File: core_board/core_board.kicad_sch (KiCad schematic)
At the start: 92 parts

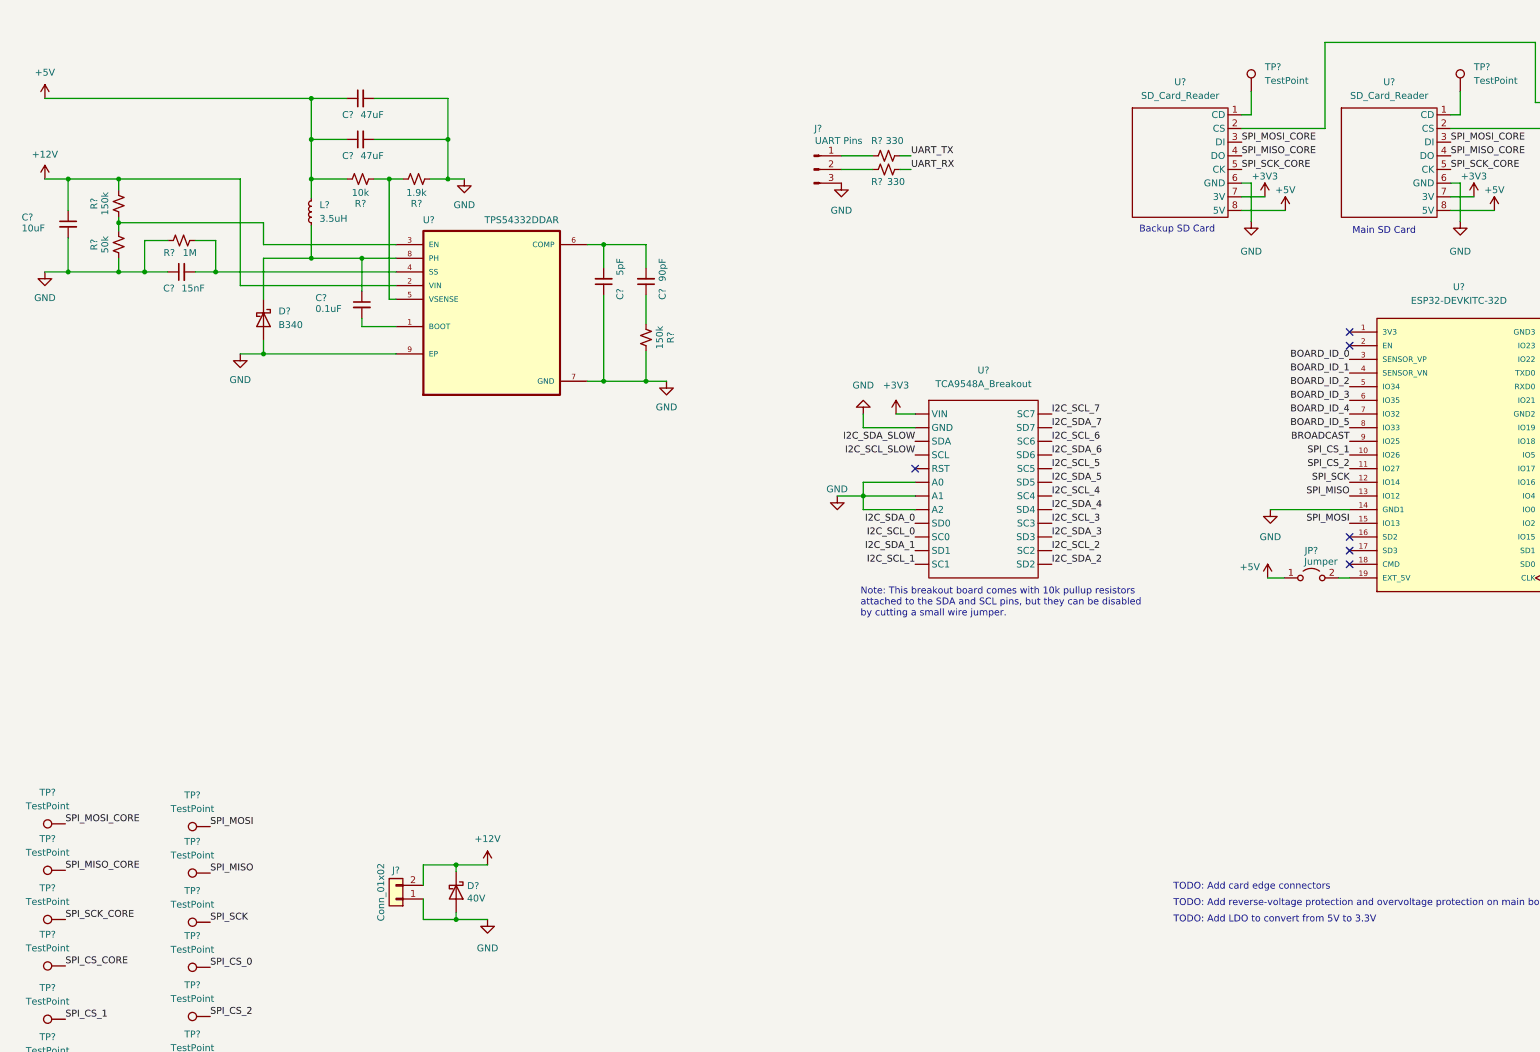
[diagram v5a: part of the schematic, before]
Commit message: added LDO
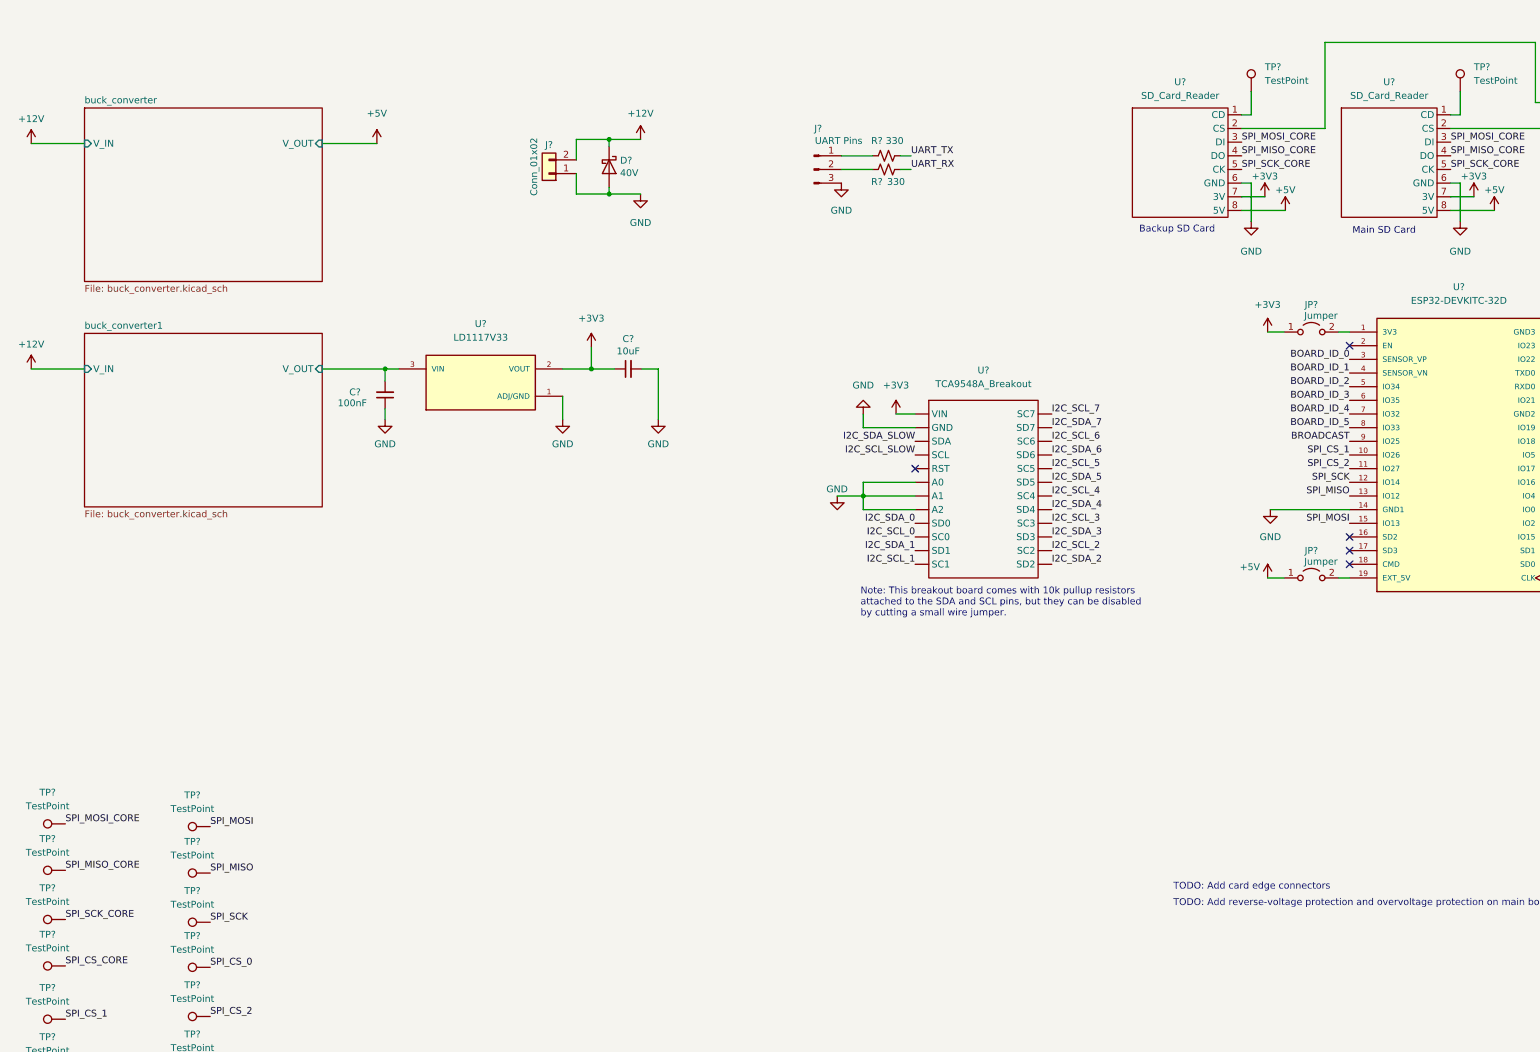
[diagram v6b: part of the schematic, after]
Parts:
- removed C? (x2): 47uF, symbol Device:C_Small
- removed C?: 90pF, symbol Device:C_Small
- removed C?: 5pF, symbol Device:C_Small
- removed C?: 10uF, symbol Device:C_Small
- removed C?: 0.1uF, symbol Device:C_Small
- removed C?: 15nF, symbol Device:C_Small
- removed D?: B340, Diode_SMD:D_SMC, symbol Diode:B340
- removed L?: 3.5uH, symbol Device:L_Small
- removed R? (x2): 150k, symbol Device:R_Small_US
- removed R?: 1M, symbol Device:R_Small_US
- removed R?: 50k, symbol Device:R_Small_US
- removed R?: 1.9k, symbol Device:R_Small_US
- removed R?: 10k, symbol Device:R_Small_US
- removed U?: TPS54332DDAR, VREG_LM5017MR/NOPB, symbol TPS54332DDAR:TPS54332DDAR
- added C?: 100nF, symbol Device:C_Small
- added C?: 10uF, symbol Device:C_Small
- added JP?: Jumper, symbol Jumper:Jumper_2_Open
- added U?: LD1117V33, TO255P1020X450X1968-3, symbol LD1117V33:LD1117V33
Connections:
- net +3V3: now also C?.1, JP?.1 (A), U?.2 (VOUT)
- net GND: now also C?.1, C?.2, U?.1 (ADJ/GND)
- net at U?.1 (3V3): now also JP?.2 (B)
- new net buck_converter1/V_OUT: C?.2, U?.3 (VIN)
- no-connect marks 11 -> 10
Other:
- added sheet buck_converter (buck_converter.kicad_sch)
- added sheet buck_converter1 (buck_converter.kicad_sch)
- note removed: "TODO: Add LDO to convert from 5V to 3.3V"
- moved on the sheet: D?, J?

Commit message: small changes
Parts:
- removed D?: 40V, Diode_SMD:D_0603_1608Metric, symbol Device:D_Schottky
- added D?: D_Zener, symbol Device:D_Zener
- added D?: D_Schottky, symbol Device:D_Schottky
- added R? (x2): 4.7k, symbol Device:R_Small_US
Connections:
- net +12V: now also D?.1 (K), D?.1 (K); no longer J?.2 (Pin_2)
- net +3V3: now also R?.2, R?.2; no longer JP?.1 (A), JP?.1 (A), U?.2 (CS), U?.2 (CS)
- net GND: now also D?.2 (A)
- new net: JP?.1 (A), R?.1, U?.2 (CS) (x2)
- new net: D?.2 (A), J?.2 (Pin_2)
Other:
- note removed: "TODO: Add card edge connectors"
- note removed: "TODO: Add reverse-voltage protection and overvoltage protection on main board"
- moved on the sheet: C?, J?, JP?, R?, TP?, U?

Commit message: added PCIE connectors
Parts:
- removed C?: 10uF, symbol Device:C_Small
- added C?: 10uF, symbol Device:C_Small
- added J? (x8): PCIE-LP-01-01-F-DV-A-TR, SAMTEC_PCIE-LP-01-01-F-DV-A-TR, symbol PCIE_Socket:PCIE-LP-01-01-F-DV-A-TR
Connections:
- net +12V: now also J?.A16, J?.A16, J?.A16, J?.A16, J?.A16, J?.A16, J?.A16, J?.A16, J?.A17, J?.A17, J?.A17, J?.A17, J?.A17, J?.A17, J?.A17, J?.A17, J?.A18, J?.A18, J?.A18, J?.A18, J?.A18, J?.A18, J?.A18, J?.A18, J?.B16, J?.B16, J?.B16, J?.B16, J?.B16, J?.B16, J?.B16, J?.B16, J?.B17, J?.B17, J?.B17, J?.B17, J?.B17, J?.B17, J?.B17, J?.B17, J?.B18, J?.B18, J?.B18, J?.B18, J?.B18, J?.B18, J?.B18, J?.B18
- net +3V3: now also C?.2, J?.A12, J?.A12, J?.A12, J?.A12, J?.A12, J?.A12, J?.A12, J?.A12, J?.A13, J?.A13, J?.A13, J?.A13, J?.A13, J?.A13, J?.A13, J?.A13
- net +5V: now also J?.B12, J?.B12, J?.B12, J?.B12, J?.B12, J?.B12, J?.B12, J?.B12, J?.B13, J?.B13, J?.B13, J?.B13, J?.B13, J?.B13, J?.B13, J?.B13
- net BOARD_ID_0: now also J?.B11
- net BOARD_ID_1: now also J?.B11
- net BOARD_ID_2: now also J?.B11
- net BOARD_ID_3: now also J?.B11
- net BOARD_ID_4: now also J?.B11
- net BOARD_ID_5: now also J?.B11
- net BOARD_ID_6: now also J?.B11
- net BOARD_ID_7: now also J?.B11
- net BROADCAST: now also J?.A11, J?.A11, J?.A11, J?.A11, J?.A11, J?.A11, J?.A11, J?.A11
- net GND: now also C?.1, J?.A02, J?.A02, J?.A02, J?.A02, J?.A02, J?.A02, J?.A02, J?.A02, J?.A04, J?.A04, J?.A04, J?.A04, J?.A04, J?.A04, J?.A04, J?.A04, J?.A06, J?.A06, J?.A06, J?.A06, J?.A06, J?.A06, J?.A06, J?.A06, J?.A08, J?.A08, J?.A08, J?.A08, J?.A08, J?.A08, J?.A08, J?.A08, J?.A10, J?.A10, J?.A10, J?.A10, J?.A10, J?.A10, J?.A10, J?.A10, J?.A14, J?.A14, J?.A14, J?.A14, J?.A14, J?.A14, J?.A14, J?.A14, J?.A15, J?.A15, J?.A15, J?.A15, J?.A15, J?.A15, J?.A15, J?.A15, J?.B01, J?.B01, J?.B01, J?.B01, J?.B01, J?.B01, J?.B01, J?.B01, J?.B03, J?.B03, J?.B03, J?.B03, J?.B03, J?.B03, J?.B03, J?.B03, J?.B05, J?.B05, J?.B05, J?.B05, J?.B05, J?.B05, J?.B05, J?.B05, J?.B07, J?.B07, J?.B07, J?.B07, J?.B07, J?.B07, J?.B07, J?.B07, J?.B09, J?.B09, J?.B09, J?.B09, J?.B09, J?.B09, J?.B09, J?.B09, J?.B14, J?.B14, J?.B14, J?.B14, J?.B14, J?.B14, J?.B14, J?.B14, J?.B15, J?.B15, J?.B15, J?.B15, J?.B15, J?.B15, J?.B15, J?.B15
- net I2C_SCL_0: now also J?.A03
- net I2C_SCL_1: now also J?.A03
- net I2C_SCL_2: now also J?.A03
- net I2C_SCL_3: now also J?.A03
- net I2C_SCL_4: now also J?.A03
- net I2C_SCL_5: now also J?.A03
- net I2C_SCL_6: now also J?.A03
- net I2C_SCL_7: now also J?.A03
- net I2C_SCL_FAST: now also J?.B04, J?.B04, J?.B04, J?.B04, J?.B04, J?.B04, J?.B04, J?.B04
- net I2C_SDA_0: now also J?.A01
- net I2C_SDA_1: now also J?.A01
- net I2C_SDA_2: now also J?.A01
- net I2C_SDA_3: now also J?.A01
- net I2C_SDA_4: now also J?.A01
- net I2C_SDA_5: now also J?.A01
- net I2C_SDA_6: now also J?.A01
- net I2C_SDA_7: now also J?.A01
- net I2C_SDA_FAST: now also J?.B02, J?.B02, J?.B02, J?.B02, J?.B02, J?.B02, J?.B02, J?.B02
- net SPI_CS_0: now also J?.B06, J?.B06, J?.B06, J?.B06, J?.B06, J?.B06, J?.B06, J?.B06
- net SPI_CS_1: now also J?.B08, J?.B08, J?.B08, J?.B08, J?.B08, J?.B08, J?.B08, J?.B08
- net SPI_CS_2: now also J?.B10, J?.B10, J?.B10, J?.B10, J?.B10, J?.B10, J?.B10, J?.B10
- net SPI_MISO: now also J?.A05, J?.A05, J?.A05, J?.A05, J?.A05, J?.A05, J?.A05, J?.A05
- net SPI_MOSI: now also J?.A09, J?.A09, J?.A09, J?.A09, J?.A09, J?.A09, J?.A09, J?.A09
- net SPI_SCK: now also J?.A07, J?.A07, J?.A07, J?.A07, J?.A07, J?.A07, J?.A07, J?.A07
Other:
- note removed: "Note: This breakout board comes with 10k pullup resistors attached to the SDA and SCL pins, but they can be disabled by cutting a small wire jumper."
- moved on the sheet: C?, D?, J?, JP?, R?, TP?, U?
